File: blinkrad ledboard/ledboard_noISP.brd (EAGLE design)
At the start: 10.3 x 17.1 mm, 17 parts, among them IC1 TINY13-20SSU

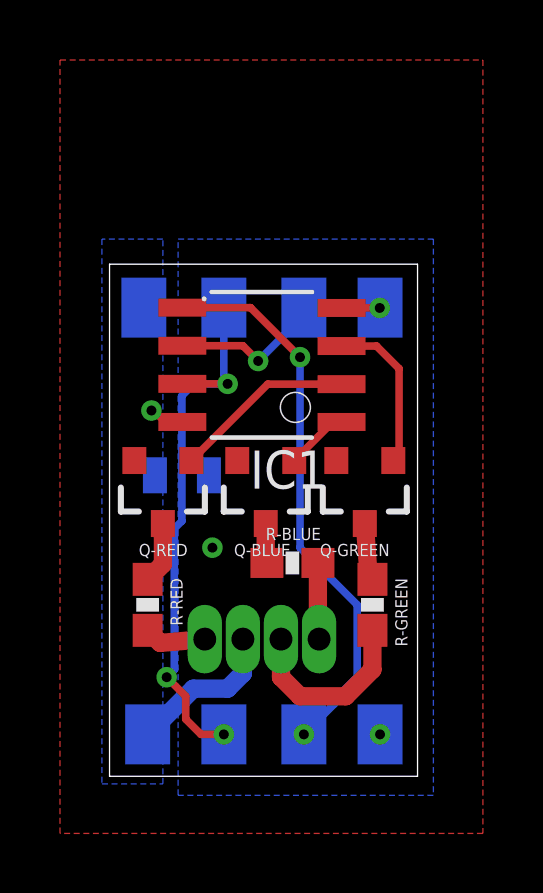
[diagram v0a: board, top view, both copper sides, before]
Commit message: MASSIVE ERROR, USE N FET
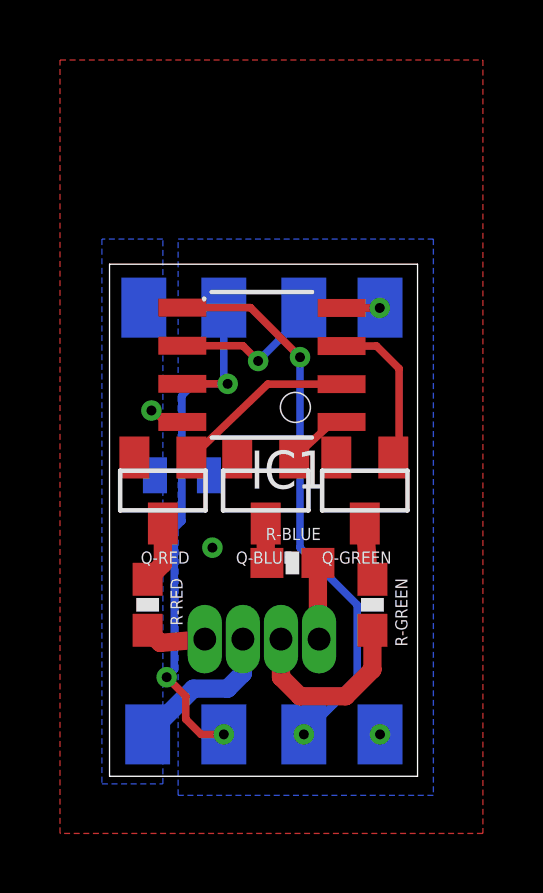
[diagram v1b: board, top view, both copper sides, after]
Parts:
- Q-BLUE, Q-GREEN, Q-RED: device SparkFun-DiscreteSemi:SOT23-3 -> SparkFun-DiscreteSemi:SOT23
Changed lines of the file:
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@@
 <attribute name="PROD_ID" value="DIO-10631" x="-20.32" y="0.508" size="1.778" layer="28" rot="MR0" display="off"/>
 </element>
-<element name="Q-RED" library="SparkFun-DiscreteSemi" package="SOT23-3" value="30V, 2.5A" x="1.778" y="9.271" rot="R180">
-<attribute name="PROD_ID" value="TRANS-11308" x="-26.162" y="30.861" size="1.778" layer="27" rot="R180" display="off"/>
+<element name="Q-RED" library="SparkFun-DiscreteSemi" package="SOT23" value="30V, 2.5A" x="1.778" y="9.271" rot="R180">
+<attribute name="PROD_ID" value="TRANS-08345" x="-26.162" y="30.861" size="1.778" layer="27" rot="R180" display="off"/>
 </element>
-<element name="Q-GREEN" library="SparkFun-DiscreteSemi" package="SOT23-3" value="30V, 2.5A" x="8.509" y="9.271" rot="R180">
-<attribute name="PROD_ID" value="TRANS-11308" x="-11.811" y="30.861" size="1.778" layer="27" rot="R180" display="off"/>
+<element name="Q-GREEN" library="SparkFun-DiscreteSemi" package="SOT23" value="30V, 2.5A" x="8.509" y="9.271" rot="R180">
+<attribute name="PROD_ID" value="TRANS-08345" x="-11.811" y="30.861" size="1.778" layer="27" rot="R180" display="off"/>
 </element>
-<element name="Q-BLUE" library="SparkFun-DiscreteSemi" package="SOT23-3" value="30V, 2.5A" x="5.207" y="9.271" rot="R180">
-<attribute name="PROD_ID" value="TRANS-11308" x="-18.923" y="30.861" size="1.778" layer="27" rot="R180" display="off"/>
+<element name="Q-BLUE" library="SparkFun-DiscreteSemi" package="SOT23" value="30V, 2.5A" x="5.207" y="9.271" rot="R180">
+<attribute name="PROD_ID" value="TRANS-08345" x="-18.923" y="30.861" size="1.778" layer="27" rot="R180" display="off"/>
 </element>
 <element name="R-RED" library="SparkFun-Resistors" package="0603-RES" value="" x="1.27" y="5.461" rot="R270"/>
@@
 <contactref element="Q-BLUE" pad="1"/>
 <wire x1="7.734" y1="11.557" x2="7.443" y2="11.557" width="0.254" layer="1"/>
-<wire x1="7.443" y1="11.557" x2="6.157" y2="10.271" width="0.254" layer="1"/>
+<wire x1="7.443" y1="11.557" x2="6.157" y2="10.371" width="0.254" layer="1"/>
 </signal>
 <signal name="VCC">
@@
 <contactref element="Q-RED" pad="1"/>
 <wire x1="7.734" y1="12.817" x2="5.274" y2="12.817" width="0.254" layer="1"/>
-<wire x1="5.274" y1="12.817" x2="2.728" y2="10.271" width="0.254" layer="1"/>
+<wire x1="5.274" y1="12.817" x2="2.728" y2="10.371" width="0.254" layer="1"/>
 </signal>
 <signal name="GREEN">
@@
 <wire x1="8.9" y1="14.087" x2="9.652" y2="13.335" width="0.254" layer="1"/>
 <wire x1="9.652" y1="13.335" x2="9.652" y2="10.459" width="0.254" layer="1"/>
-<wire x1="9.652" y1="10.459" x2="9.459" y2="10.271" width="0.254" layer="1"/>
+<wire x1="9.652" y1="10.459" x2="9.459" y2="10.371" width="0.254" layer="1"/>
 </signal>
 </signals>
